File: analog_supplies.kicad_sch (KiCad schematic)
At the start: 33 parts, among them Q1 PMOS, Q4 2NPN, U24 LDO-ADJ

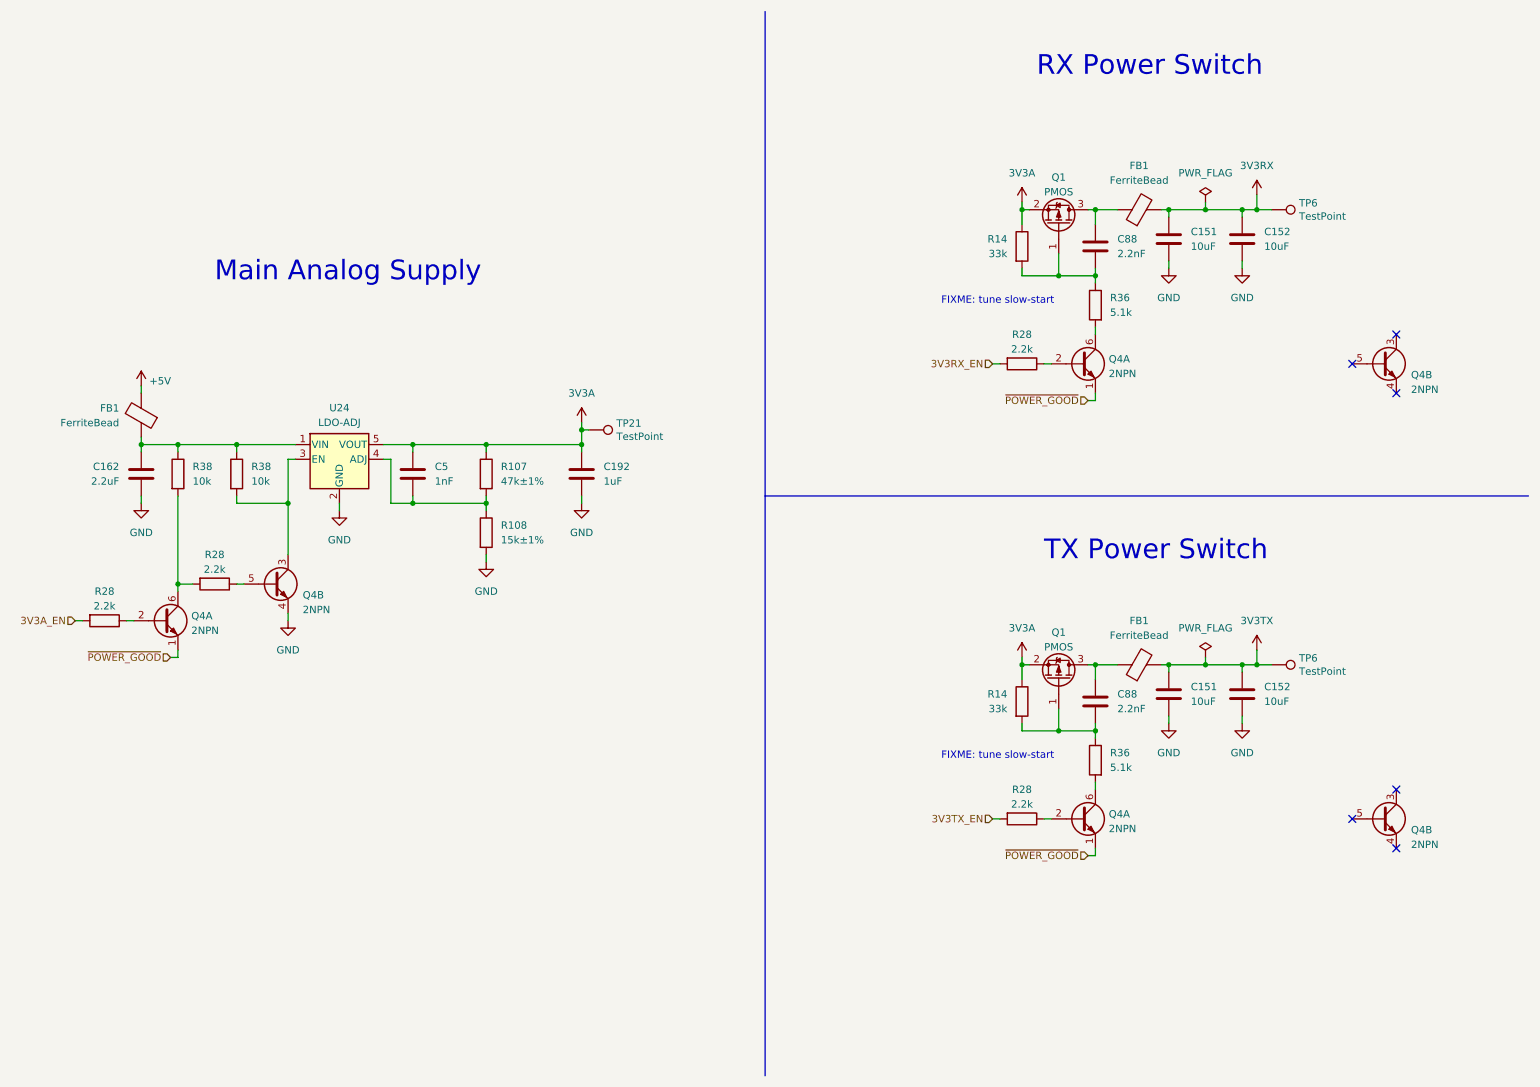
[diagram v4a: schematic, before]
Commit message: complete initial layout
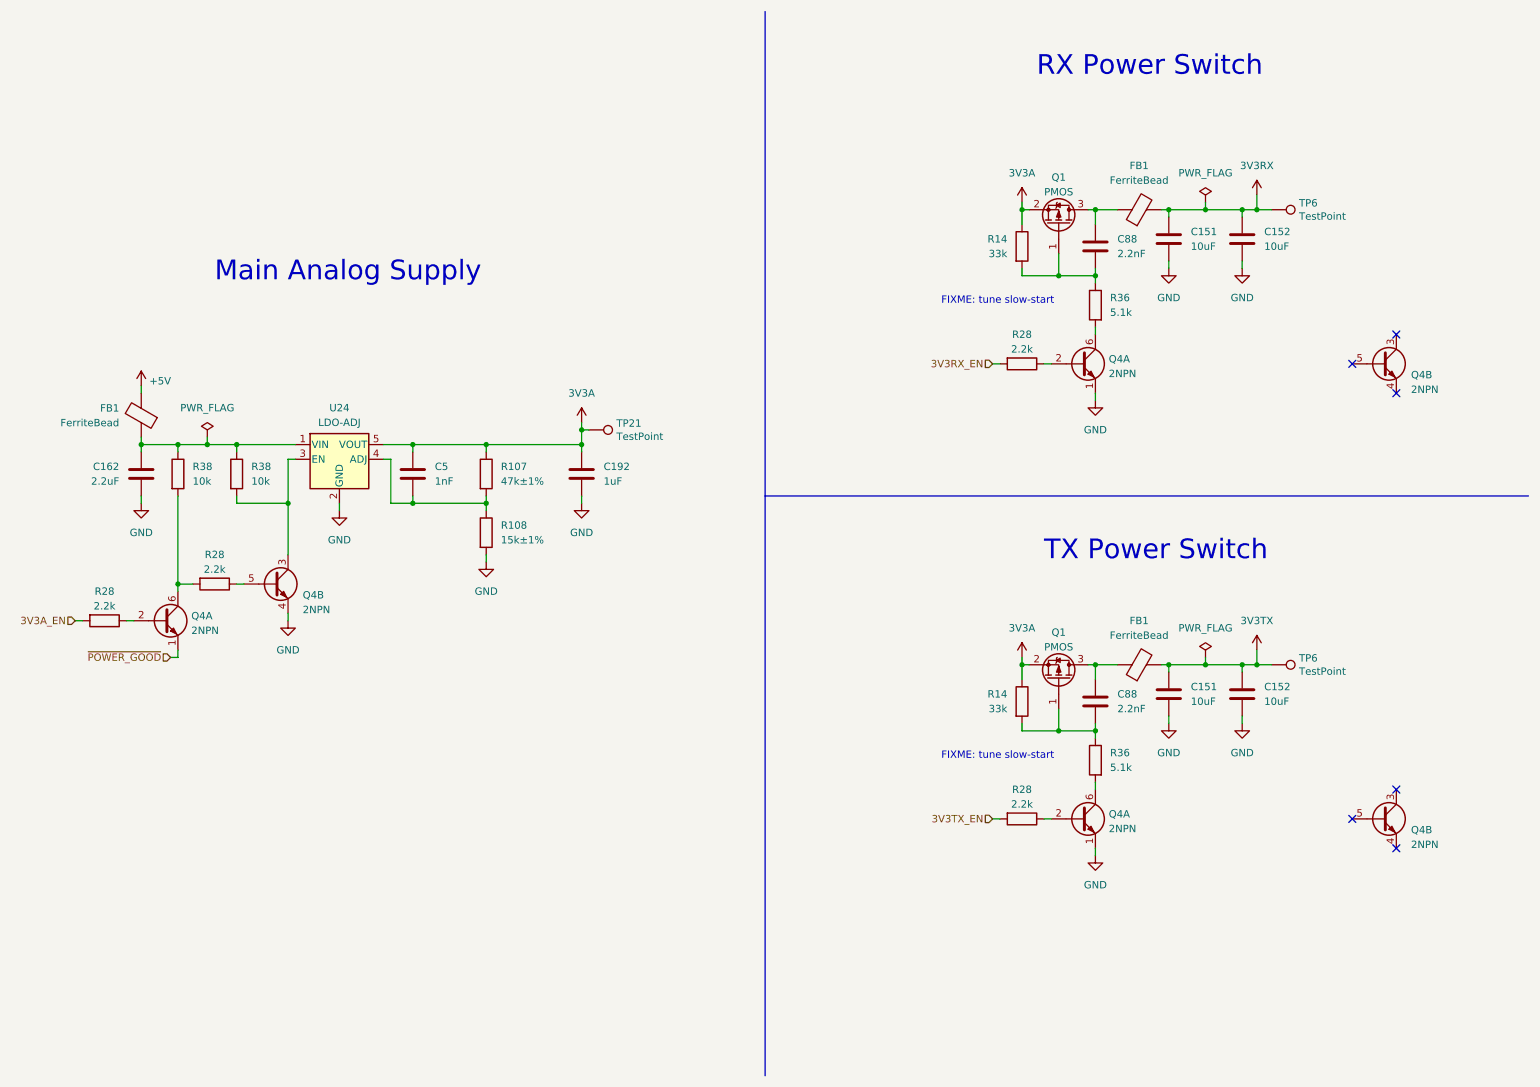
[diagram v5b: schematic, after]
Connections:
- net GND: now also Q4.1 (E1), Q4.1 (E1)
- net ~{POWER_GOOD}: no longer Q4.1 (E1), Q4.1 (E1)
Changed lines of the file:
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@@
   (junction (at 104.14 87.63) (diameter 0) (color 0 0 0 0)
+  )
+  (junction (at 55.88 87.63) (diameter 0) (color 0 0 0 0)
   )
   (junction (at 209.55 46.99) (diameter 0) (color 0 0 0 0)
@@
     (stroke (width 0) (type default))
   )
+  (wire (pts (xy 55.88 87.63) (xy 60.96 87.63))
+    (stroke (width 0) (type default))
+  )
   (wire (pts (xy 200.66 73.66) (xy 201.93 73.66))
     (stroke (width 0) (type default))
@@
     (stroke (width 0) (type default))
   )
+  (wire (pts (xy 91.44 96.52) (xy 91.44 97.79))
+    (stroke (width 0) (type default))
+  )
+  (wire (pts (xy 200.66 152.4) (xy 201.93 152.4))
+    (stroke (width 0) (type default))
+  )
+  (wire (pts (xy 209.55 125.73) (xy 213.36 125.73))
+    (stroke (width 0) (type default))
+  )
+  (wire (pts (xy 55.88 86.36) (xy 55.88 87.63))
+    (stroke (width 0) (type default))
+  )
+  (wire (pts (xy 228.6 124.46) (xy 228.6 125.73))
+    (stroke (width 0) (type default))
+  )
+  (wire (pts (xy 209.55 137.16) (xy 209.55 138.43))
+    (stroke (width 0) (type default))
+  )
+  (wire (pts (xy 196.85 58.42) (xy 203.2 58.42))
+    (stroke (width 0) (type default))
+  )
+  (wire (pts (xy 120.65 85.09) (xy 120.65 87.63))
+    (stroke (width 0) (type default))
+  )
+  (wire (pts (xy 104.14 87.63) (xy 120.65 87.63))
+    (stroke (width 0) (type default))
+  )
   (wire (pts (xy 209.55 157.48) (xy 209.55 158.75))
     (stroke (width 0) (type default))
   )
+  (wire (pts (xy 209.55 46.99) (xy 213.36 46.99))
+    (stroke (width 0) (type default))
+  )
+  (wire (pts (xy 50.8 123.19) (xy 50.8 124.46))
+    (stroke (width 0) (type default))
+  )
+  (wire (pts (xy 203.2 137.16) (xy 209.55 137.16))
+    (stroke (width 0) (type default))
+  )
+  (wire (pts (xy 60.96 87.63) (xy 60.96 88.9))
+    (stroke (width 0) (type default))
+  )
+  (wire (pts (xy 121.92 85.09) (xy 120.65 85.09))
+    (stroke (width 0) (type default))
+  )
+  (wire (pts (xy 120.65 83.82) (xy 120.65 85.09))
+    (stroke (width 0) (type default))
+  )
+  (wire (pts (xy 203.2 54.61) (xy 203.2 58.42))
+    (stroke (width 0) (type default))
+  )
+  (wire (pts (xy 50.8 111.76) (xy 50.8 113.03))
+    (stroke (width 0) (type default))
+  )
+  (wire (pts (xy 60.96 97.79) (xy 69.85 97.79))
+    (stroke (width 0) (type default))
+  )
+  (wire (pts (xy 228.6 125.73) (xy 234.95 125.73))
+    (stroke (width 0) (type default))
+  )
+  (polyline (pts (xy 152.4 96.52) (xy 284.48 96.52))
+    (stroke (width 0) (type default))
+  )
   (wire (pts (xy 209.55 78.74) (xy 209.55 80.01))
     (stroke (width 0) (type default))
   )
-  (wire (pts (xy 91.44 96.52) (xy 91.44 97.79))
-    (stroke (width 0) (type default))
-  )
-  (wire (pts (xy 200.66 152.4) (xy 201.93 152.4))
-    (stroke (width 0) (type default))
-  )
-  (wire (pts (xy 209.55 125.73) (xy 213.36 125.73))
-    (stroke (width 0) (type default))
-  )
-  (wire (pts (xy 208.28 80.01) (xy 209.55 80.01))
-    (stroke (width 0) (type default))
-  )
-  (wire (pts (xy 228.6 124.46) (xy 228.6 125.73))
-    (stroke (width 0) (type default))
-  )
-  (wire (pts (xy 209.55 137.16) (xy 209.55 138.43))
-    (stroke (width 0) (type default))
-  )
-  (wire (pts (xy 196.85 58.42) (xy 203.2 58.42))
-    (stroke (width 0) (type default))
-  )
-  (wire (pts (xy 120.65 85.09) (xy 120.65 87.63))
-    (stroke (width 0) (type default))
-  )
-  (wire (pts (xy 104.14 87.63) (xy 120.65 87.63))
-    (stroke (width 0) (type default))
-  )
-  (wire (pts (xy 209.55 46.99) (xy 213.36 46.99))
-    (stroke (width 0) (type default))
-  )
-  (wire (pts (xy 50.8 123.19) (xy 50.8 124.46))
-    (stroke (width 0) (type default))
-  )
-  (wire (pts (xy 203.2 137.16) (xy 209.55 137.16))
-    (stroke (width 0) (type default))
-  )
-  (wire (pts (xy 60.96 87.63) (xy 60.96 88.9))
-    (stroke (width 0) (type default))
-  )
-  (wire (pts (xy 121.92 85.09) (xy 120.65 85.09))
-    (stroke (width 0) (type default))
-  )
-  (wire (pts (xy 120.65 83.82) (xy 120.65 85.09))
-    (stroke (width 0) (type default))
-  )
-  (wire (pts (xy 203.2 54.61) (xy 203.2 58.42))
-    (stroke (width 0) (type default))
-  )
-  (wire (pts (xy 50.8 111.76) (xy 50.8 113.03))
-    (stroke (width 0) (type default))
-  )
-  (wire (pts (xy 60.96 97.79) (xy 69.85 97.79))
-    (stroke (width 0) (type default))
-  )
-  (wire (pts (xy 228.6 125.73) (xy 234.95 125.73))
-    (stroke (width 0) (type default))
-  )
-  (polyline (pts (xy 152.4 96.52) (xy 284.48 96.52))
-    (stroke (width 0) (type default))
-  )
   (wire (pts (xy 209.55 146.05) (xy 209.55 147.32))
     (stroke (width 0) (type default))
@@
     (stroke (width 0) (type default))
   )
-  (wire (pts (xy 50.8 87.63) (xy 60.96 87.63))
+  (wire (pts (xy 50.8 87.63) (xy 55.88 87.63))
     (stroke (width 0) (type default))
   )
@@
   )
   (wire (pts (xy 228.6 46.99) (xy 234.95 46.99))
-    (stroke (width 0) (type default))
-  )
-  (wire (pts (xy 208.28 158.75) (xy 209.55 158.75))
     (stroke (width 0) (type default))
   )
@@
     (effects (font (size 1.27 1.27)) (justify right))
   )
-  (hierarchical_label "~{POWER_GOOD}" (shape input) (at 208.28 158.75 180) (fields_autoplaced)
-    (effects (font (size 1.27 1.27)) (justify right))
-  )
   (hierarchical_label "3V3RX_EN" (shape input) (at 191.77 73.66 180) (fields_autoplaced)
     (effects (font (size 1.27 1.27)) (justify right))
   )
   (hierarchical_label "3V3A_EN" (shape input) (at 33.02 118.11 180) (fields_autoplaced)
-    (effects (font (size 1.27 1.27)) (justify right))
-  )
-  (hierarchical_label "~{POWER_GOOD}" (shape input) (at 208.28 80.01 180) (fields_autoplaced)
     (effects (font (size 1.27 1.27)) (justify right))
   )
@@
     )
   )
+  (symbol (lib_name "GND_2") (lib_id "power:GND") (at 209.55 158.75 0) (unit 1)
+    (in_bom yes) (on_board yes) (dnp no) (fields_autoplaced)
+    (property "Reference" "#PWR0190" (at 209.55 165.1 0)
+      (effects (font (size 1.27 1.27)) hide)
+    )
+    (property "Value" "GND" (at 209.55 163.83 0)
+      (effects (font (size 1.27 1.27)))
+    )
+    (property "Footprint" "" (at 209.55 158.75 0)
+      (effects (font (size 1.27 1.27)) hide)
+    )
+    (property "Datasheet" "" (at 209.55 158.75 0)
+      (effects (font (size 1.27 1.27)) hide)
+    )
+    (pin "1")
+    (instances
+      (project "mainboard"
+        (path "/fb621148-8145-4217-9712-738e1b5a4823/4ec621be-184d-4855-a96d-f6fa2a788a77"
+          (reference "#PWR0190") (unit 1)
+        )
+        (path "/fb621148-8145-4217-9712-738e1b5a4823/4ec621be-184d-4855-a96d-f6fa2a788a77/6aa278c8-8281-4438-81b7-90e6d7ac4f12"
+          (reference "#PWR0276") (unit 1)
+        )
+        (path "/fb621148-8145-4217-9712-738e1b5a4823/85575ef9-3107-418a-95d7-1ff02b595e8d"
+          (reference "#PWR0319") (unit 1)
+        )
+      )
+    )
+  )
   (symbol (lib_name "GND_2") (lib_id "power:GND") (at 234.95 57.15 0) (unit 1)
     (in_bom yes) (on_board yes) (dnp no) (fields_autoplaced)
@@
         (path "/fb621148-8145-4217-9712-738e1b5a4823/85575ef9-3107-418a-95d7-1ff02b595e8d"
           (reference "TP13") (unit 1)
+        )
+      )
+    )
+  )
+  (symbol (lib_id "power:PWR_FLAG") (at 55.88 86.36 0) (unit 1)
+    (in_bom yes) (on_board yes) (dnp no) (fields_autoplaced)
+    (property "Reference" "#FLG02" (at 55.88 84.455 0)
+      (effects (font (size 1.27 1.27)) hide)
+    )
+    (property "Value" "PWR_FLAG" (at 55.88 81.28 0)
+      (effects (font (size 1.27 1.27)))
+    )
+    (property "Footprint" "" (at 55.88 86.36 0)
+      (effects (font (size 1.27 1.27)) hide)
+    )
+    (property "Datasheet" "~" (at 55.88 86.36 0)
+      (effects (font (size 1.27 1.27)) hide)
+    )
+    (pin "1")
+    (instances
+      (project "mainboard"
+        (path "/fb621148-8145-4217-9712-738e1b5a4823/4ec621be-184d-4855-a96d-f6fa2a788a77/90da2209-0e18-4bd4-8ef6-3d6f9ed46ff8"
+          (reference "#FLG02") (unit 1)
+        )
+        (path "/fb621148-8145-4217-9712-738e1b5a4823/85575ef9-3107-418a-95d7-1ff02b595e8d"
+          (reference "#FLG06") (unit 1)
         )
       )
@@
         )
       )
+    )
+  )
+  (symbol (lib_name "GND_2") (lib_id "power:GND") (at 209.55 80.01 0) (unit 1)
+    (in_bom yes) (on_board yes) (dnp no) (fields_autoplaced)
+    (property "Reference" "#PWR0190" (at 209.55 86.36 0)
+      (effects (font (size 1.27 1.27)) hide)
+    )
+    (property "Value" "GND" (at 209.55 85.09 0)
+      (effects (font (size 1.27 1.27)))
+    )
+    (property "Footprint" "" (at 209.55 80.01 0)
+      (effects (font (size 1.27 1.27)) hide)
+    )
+    (property "Datasheet" "" (at 209.55 80.01 0)
+      (effects (font (size 1.27 1.27)) hide)
+    )
+    (pin "1")
+    (instances
+      (project "mainboard"
+        (path "/fb621148-8145-4217-9712-738e1b5a4823/4ec621be-184d-4855-a96d-f6fa2a788a77"
+          (reference "#PWR0190") (unit 1)
+        )
+        (path "/fb621148-8145-4217-9712-738e1b5a4823/4ec621be-184d-4855-a96d-f6fa2a788a77/6aa278c8-8281-4438-81b7-90e6d7ac4f12"
+          (reference "#PWR0276") (unit 1)
+        )
+        (path "/fb621148-8145-4217-9712-738e1b5a4823/4ec621be-184d-4855-a96d-f6fa2a788a77/90da2209-0e18-4bd4-8ef6-3d6f9ed46ff8"
+          (reference "#PWR0236") (unit 1)
+        )
+        (path "/fb621148-8145-4217-9712-738e1b5a4823/85575ef9-3107-418a-95d7-1ff02b595e8d"
+          (reference "#PWR0283") (unit 1)
+        )
+      )
